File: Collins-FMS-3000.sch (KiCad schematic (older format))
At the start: 3 parts, among them J1 Conn_01x04_Male, U1 MCP23017_SO, U2 MCP23017_SO

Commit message: Add LED driver chip
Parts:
- added C1, C3, C5, C7: 1uF, Capacitor_SMD:C_0402_1005Metric, symbol Device:C_Small
- added C2, C4, C6, C8: 0.1uF, Capacitor_SMD:C_0402_1005Metric, symbol Device:C_Small
- added R1, R2, R3, R4, R5, R6: 2k, Resistor_SMD:R_0402_1005Metric, symbol Device:R_Small
- added R7: 30k, Resistor_SMD:R_0402_1005Metric, symbol Device:R_Small
- added R8: 10k, Resistor_SMD:R_0402_1005Metric, symbol Device:R_Small
- added U3: IS31FL3743A, Package_DFN_QFN:QFN-40-1EP_5x5mm_P0.4mm_EP3.8x3.8mm_ThermalVias, symbol Collins-FMS-3000:IS31FL3743A
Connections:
- wire segments 41 -> 106
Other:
- note added: "I2C addresss: 0x2C"
- moved on the sheet: U1, U2

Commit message: Add LED driver and led matrix
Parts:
- added R5: 100k, symbol Device:R_Small
- R6: renamed from R5; value 2k -> 4k7
- R7: renamed from R6; value 2k -> 4k7
- renumbered R7 to R8, R8 to R9
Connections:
- wire segments 106 -> 129
- no-connect marks 13 -> 20
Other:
- note added: "Backlight LEDs"
- moved on the sheet: C5, C6, C7, C8, R6, R7, R8, R9, U3

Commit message: Add ATmega32u4 to board
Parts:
- removed J1: Conn_01x04_Male, Connector_JST:JST_XH_B4B-XH-AM_1x04_P2.50mm_Vertical, symbol Connector:Conn_01x04_Male
- C2, C4, C6, C8: value 0.1uF -> 100nf
- R5: footprint (none) -> Resistor_SMD:R_0402_1005Metric
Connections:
- wire segments 129 -> 126
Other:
- note added: "ATmega32u4 microcontroller"
- note removed: "Arduino connection"
- moved on the sheet: C1, C2, C3, C4, C5, C6, C7, C8, R1, R2, R3, R4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

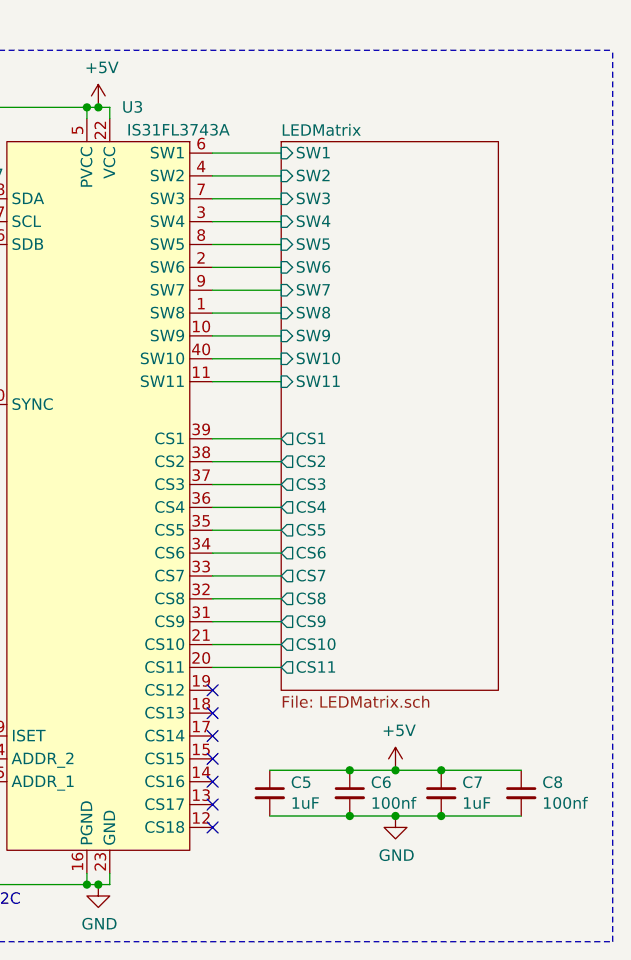
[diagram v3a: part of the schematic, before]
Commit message: Redo the LED matrix
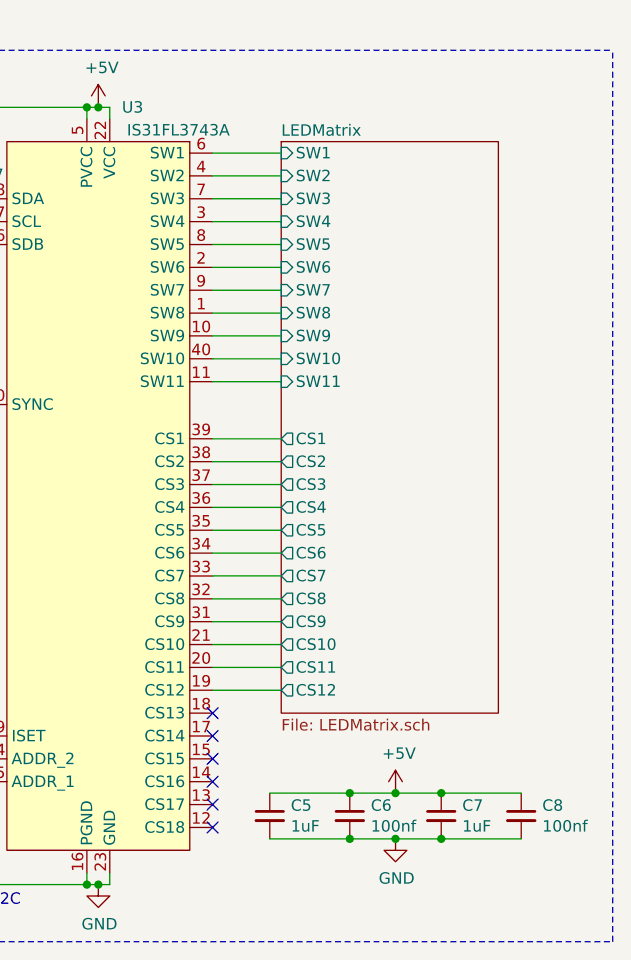
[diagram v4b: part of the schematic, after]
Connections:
- net LEDMatrix/CS12: now reaches U3.19 (CS12)
- no-connect marks 20 -> 19
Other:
- moved on the sheet: C5, C6, C7, C8

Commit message: Much PCB layout
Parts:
- renumbered U1 to U2, U2 to U3, U3 to U4
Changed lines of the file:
@@
 $EndSheet
 $Comp
-L Interface_Expansion:MCP23017_SO U1
+L Interface_Expansion:MCP23017_SO U2
 U 1 1 626E613B
 P 3200 2000
-F 0 "U1" H 3250 3050 50  0000 L CNN
+F 0 "U2" H 3250 3050 50  0000 L CNN
 F 1 "MCP23017_SO" H 3250 2950 50  0000 L CNN
 F 2 "Package_SO:SOIC-28W_7.5x17.9mm_P1.27mm" H 3400 1000 50  0001 L CNN
@@
 $EndComp
 $Comp
-L Interface_Expansion:MCP23017_SO U2
+L Interface_Expansion:MCP23017_SO U3
 U 1 1 626F440B
 P 5600 2000
-F 0 "U2" H 5650 3050 50  0000 L CNN
+F 0 "U3" H 5650 3050 50  0000 L CNN
 F 1 "MCP23017_SO" H 5650 2950 50  0000 L CNN
 F 2 "Package_SO:SOIC-28W_7.5x17.9mm_P1.27mm" H 5800 1000 50  0001 L CNN
@@
 Wire Notes Line
 	7100 3500 7100 650
-$Comp
-L Collins-FMS-3000:IS31FL3743A U3
-U 1 1 619107BE
-P 8550 2200
-F 0 "U3" H 8700 3500 50  0000 C CNN
-F 1 "IS31FL3743A" H 8900 3400 50  0000 C CNN
-F 2 "Package_DFN_QFN:QFN-40-1EP_5x5mm_P0.4mm_EP3.8x3.8mm_ThermalVias" H 8550 -300 50  0001 C CNN
-F 3 "https://www.lumissil.com/assets/pdf/core/IS31FL3743A_DS.pdf" H 8550 2200 50  0001 C CNN
-	1    8550 2200
-	1    0    0    -1
-$EndComp
 Wire Wire Line
 	8500 950  8500 900
@@
 Wire Wire Line
 	9350 3450 9050 3450
+$Comp
+L Collins-FMS-3000:IS31FL3743A U4
+U 1 1 619107BE
+P 8550 2200
+F 0 "U4" H 8700 3500 50  0000 C CNN
+F 1 "IS31FL3743A" H 8900 3400 50  0000 C CNN
+F 2 "Package_DFN_QFN:QFN-40-1EP_5x5mm_P0.4mm_EP3.8x3.8mm_ThermalVias" H 8550 -300 50  0001 C CNN
+F 3 "https://www.lumissil.com/assets/pdf/core/IS31FL3743A_DS.pdf" H 8550 2200 50  0001 C CNN
+	1    8550 2200
+	1    0    0    -1
+$EndComp
 $EndSCHEMATC

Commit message: Lots of PCB layout
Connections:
- net SCK renamed SCL
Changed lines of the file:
@@
 SDA
 Text GLabel 2100 1300 0    50   Input ~ 0
-SCK
+SCL
 NoConn ~ 2500 1800
 NoConn ~ 2500 1900
@@
 SDA
 Text GLabel 6850 1300 2    50   Input ~ 0
-SCK
+SCL
 $Comp
 L power:+5V #PWR03
@@
 SDA
 Text GLabel 7600 1400 0    50   Input ~ 0
-SCK
+SCL
 $Comp
 L Device:R_Small R6
@@
 F1 "ATmega32u4.sch" 50
 F2 "SDA" B R 1500 1050 50
-F3 "SCK" O R 1500 1150 50
+F3 "SCL" O R 1500 1150 50
 $EndSheet
-Text GLabel 1500 1050 2    50   BiDi ~ 0
+Text GLabel 1550 1050 2    50   BiDi ~ 0
 SDA
-Text GLabel 1500 1150 2    50   Output ~ 0
-SCK
+Text GLabel 1550 1150 2    50   Output ~ 0
+SCL
 Wire Notes Line
 	550  650  550  1650
@@
 	1    0    0    -1
 $EndComp
+Wire Wire Line
+	1500 1050 1550 1050
+Wire Wire Line
+	1500 1150 1550 1150
 $EndSCHEMATC

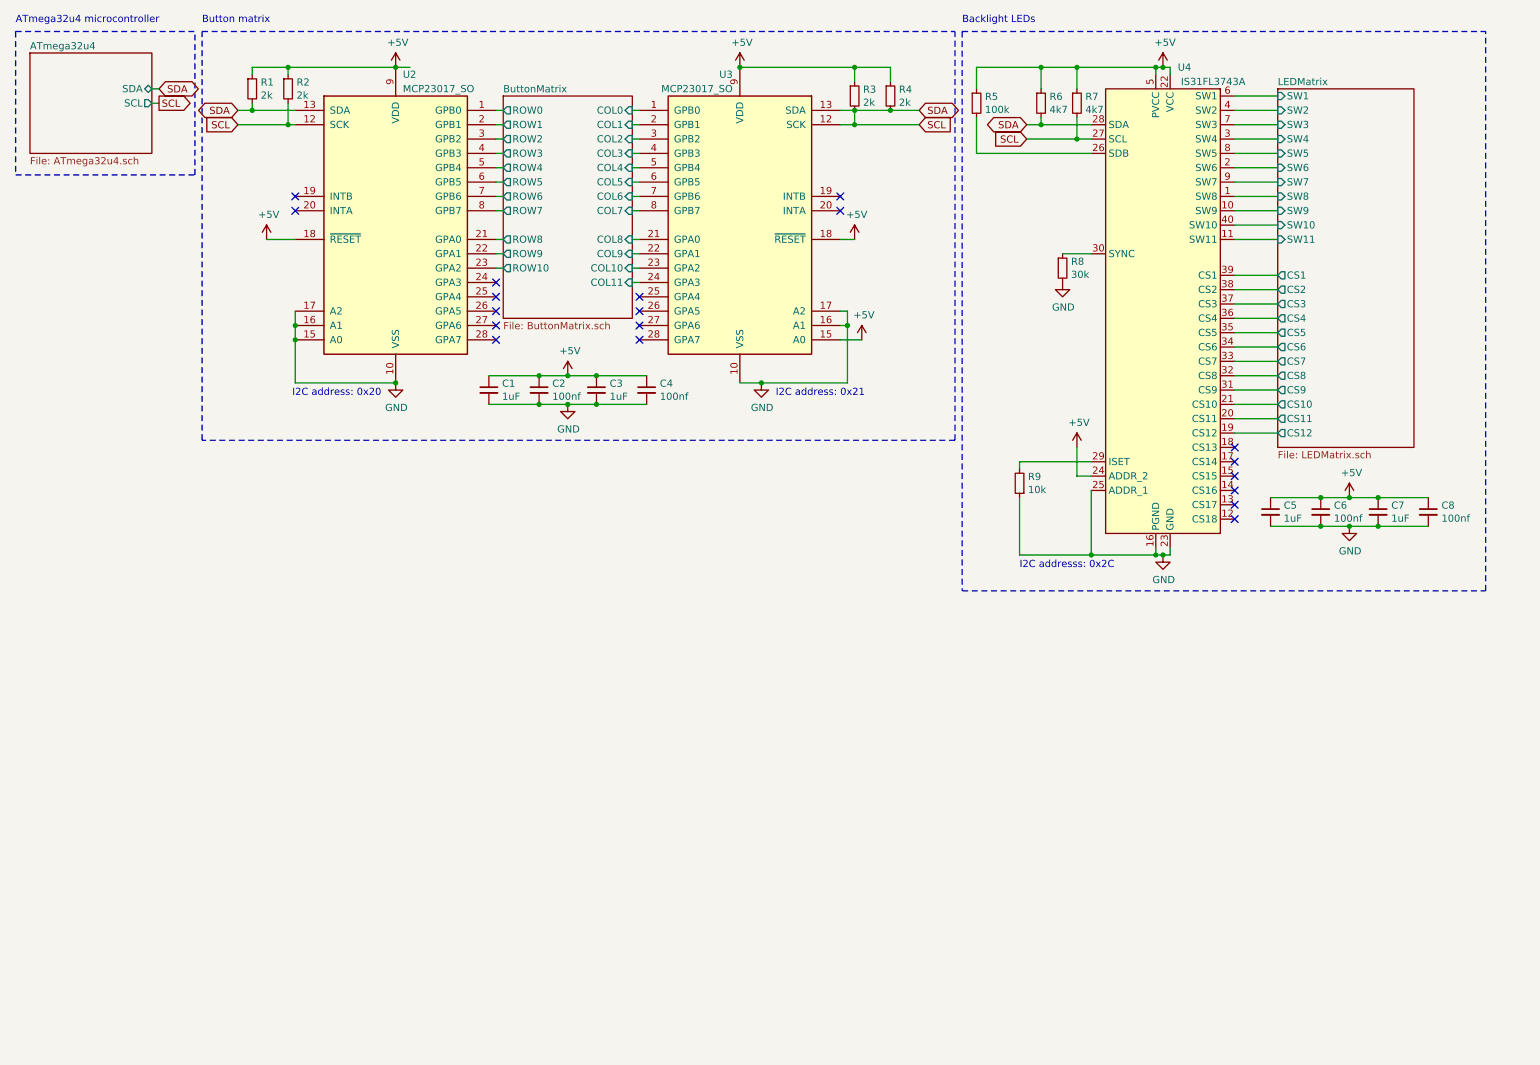
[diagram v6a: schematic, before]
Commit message: New LED chip, tons of routing on the board
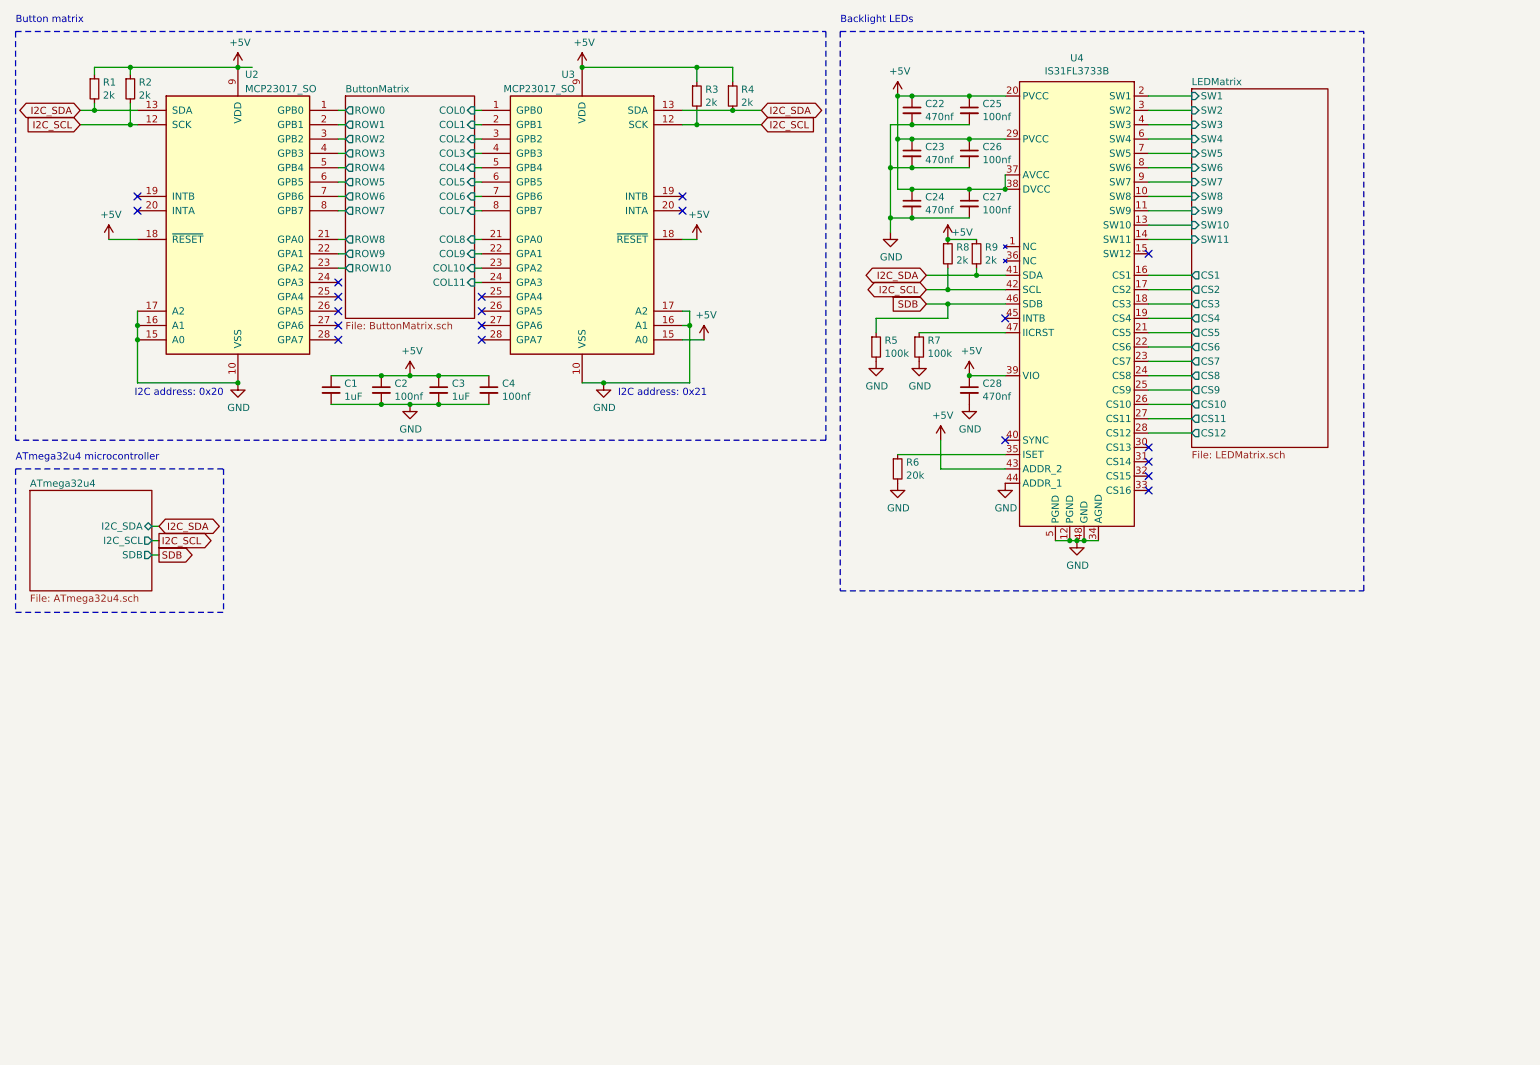
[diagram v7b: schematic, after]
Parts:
- removed C5, C7: 1uF, Capacitor_SMD:C_0402_1005Metric, symbol Device:C_Small
- removed C6, C8: 100nf, Capacitor_SMD:C_0402_1005Metric, symbol Device:C_Small
- removed U4: IS31FL3743A, Package_DFN_QFN:QFN-40-1EP_5x5mm_P0.4mm_EP3.8x3.8mm_ThermalVias, symbol Collins-FMS-3000:IS31FL3743A
- added C22, C23, C24, C28: 470nf, Capacitor_SMD:C_0402_1005Metric, symbol Device:C_Small
- added C25, C26, C27: 100nf, Capacitor_SMD:C_0402_1005Metric, symbol Device:C_Small
- added U4: IS31FL3733B, Package_QFP:TQFP-48-1EP_7x7mm_P0.5mm_EP5x5mm_ThermalVias, symbol Collins-FMS-3000:IS31FL3733B
- R6: value 4k7 -> 20k
- R7: value 4k7 -> 100k
- R8: value 30k -> 2k
- R9: value 10k -> 2k
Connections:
- net +5V: now also R8.1, R9.1, C22.1, C23.1, C24.1, C25.1, C26.1, C27.1, C28.1, U4.20 (PVCC), U4.29 (PVCC), U4.37 (AVCC), U4.38 (DVCC), U4.39 (VIO), U4.43 (ADDR_2); no longer R5.1, R6.1, R7.1
- net GND: now also R5.2, R6.2, R7.2, C22.2, C23.2, C24.2, C25.2, C26.2, C27.2, C28.2, U4.12 (PGND), U4.34 (AGND), U4.44 (ADDR_1), U4.48 (GND), U4.5 (PGND); no longer R8.2, R9.1
- net LEDMatrix/CS1: now also U4.16 (CS1)
- net LEDMatrix/CS10: now also U4.26 (CS10)
- net LEDMatrix/CS11: now also U4.27 (CS11)
- net LEDMatrix/CS12: now also U4.28 (CS12)
- net LEDMatrix/CS2: now also U4.17 (CS2)
- net LEDMatrix/CS3: now also U4.18 (CS3)
- net LEDMatrix/CS4: now also U4.19 (CS4)
- net LEDMatrix/CS5: now also U4.21 (CS5)
- net LEDMatrix/CS6: now also U4.22 (CS6)
- net LEDMatrix/CS7: now also U4.23 (CS7)
- net LEDMatrix/CS8: now also U4.24 (CS8)
- net LEDMatrix/CS9: now also U4.25 (CS9)
- net LEDMatrix/SW1: now also U4.2 (SW1)
- net LEDMatrix/SW10: now also U4.13 (SW10)
- net LEDMatrix/SW11: now also U4.14 (SW11)
- net LEDMatrix/SW2: now also U4.3 (SW2)
- net LEDMatrix/SW3: now also U4.4 (SW3)
- net LEDMatrix/SW4: now also U4.6 (SW4)
- net LEDMatrix/SW5: now also U4.7 (SW5)
- net LEDMatrix/SW6: now also U4.8 (SW6)
- net LEDMatrix/SW7: now also U4.9 (SW7)
- net LEDMatrix/SW8: now also U4.10 (SW8)
- net LEDMatrix/SW9: now also U4.11 (SW9)
- net I2C_SDA: now reaches R9.2
- net I2C_SDA: now also R1.2, R4.2, U2.13 (SDA), U3.13 (SDA), U4.41 (SDA)
- removed net SCL: R1.2, R2.2, R3.2, R4.2, R6.2, R7.2, U2.12 (SCK), U2.13 (SDA), U3.12 (SCK), U3.13 (SDA)
- new net: R7.1, U4.47 (IICRST)
- new net: R6.1, U4.35 (ISET)
- new net I2C_SCL: R2.2, R3.2, R8.2, U2.12 (SCK), U3.12 (SCK), U4.42 (SCL)
- new net SDB: R5.1, U4.46 (SDB)
- no-connect marks 19 -> 20
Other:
- note removed: "I2C addresss: 0x2C"
- moved on the sheet: C1, C2, C3, C4, R1, R2, R3, R4, U2, U3

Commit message: More routing
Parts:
- R1, R2, R3, R4, R8, R9: footprint Resistor_SMD:R_0402_1005Metric -> Resistor_SMD:R_0805_2012Metric_Pad1.20x1.40mm_HandSolder
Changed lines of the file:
@@
 F 0 "R1" H 1159 1096 50  0000 L CNN
 F 1 "2k" H 1159 1005 50  0000 L CNN
-F 2 "Resistor_SMD:R_0402_1005Metric" H 1100 1050 50  0001 C CNN
+F 2 "Resistor_SMD:R_0805_2012Metric_Pad1.20x1.40mm_HandSolder" H 1100 1050 50  0001 C CNN
 F 3 "~" H 1100 1050 50  0001 C CNN
 	1    1100 1050
@@
 F 0 "R2" H 1409 1096 50  0000 L CNN
 F 1 "2k" H 1409 1005 50  0000 L CNN
-F 2 "Resistor_SMD:R_0402_1005Metric" H 1350 1050 50  0001 C CNN
+F 2 "Resistor_SMD:R_0805_2012Metric_Pad1.20x1.40mm_HandSolder" H 1350 1050 50  0001 C CNN
 F 3 "~" H 1350 1050 50  0001 C CNN
 	1    1350 1050
@@
 F 0 "R3" H 5359 1146 50  0000 L CNN
 F 1 "2k" H 5359 1055 50  0000 L CNN
-F 2 "Resistor_SMD:R_0402_1005Metric" H 5300 1100 50  0001 C CNN
+F 2 "Resistor_SMD:R_0805_2012Metric_Pad1.20x1.40mm_HandSolder" H 5300 1100 50  0001 C CNN
 F 3 "~" H 5300 1100 50  0001 C CNN
 	1    5300 1100
@@
 F 0 "R4" H 5609 1146 50  0000 L CNN
 F 1 "2k" H 5609 1055 50  0000 L CNN
-F 2 "Resistor_SMD:R_0402_1005Metric" H 5550 1100 50  0001 C CNN
+F 2 "Resistor_SMD:R_0805_2012Metric_Pad1.20x1.40mm_HandSolder" H 5550 1100 50  0001 C CNN
 F 3 "~" H 5550 1100 50  0001 C CNN
 	1    5550 1100
@@
 F 0 "R9" H 7309 2246 50  0000 L CNN
 F 1 "2k" H 7309 2155 50  0000 L CNN
-F 2 "Resistor_SMD:R_0402_1005Metric" H 7250 2200 50  0001 C CNN
+F 2 "Resistor_SMD:R_0805_2012Metric_Pad1.20x1.40mm_HandSolder" H 7250 2200 50  0001 C CNN
 F 3 "~" H 7250 2200 50  0001 C CNN
 	1    7250 2200
@@
 F 0 "R8" H 7109 2246 50  0000 L CNN
 F 1 "2k" H 7109 2155 50  0000 L CNN
-F 2 "Resistor_SMD:R_0402_1005Metric" H 7050 2200 50  0001 C CNN
+F 2 "Resistor_SMD:R_0805_2012Metric_Pad1.20x1.40mm_HandSolder" H 7050 2200 50  0001 C CNN
 F 3 "~" H 7050 2200 50  0001 C CNN
 	1    7050 2200
